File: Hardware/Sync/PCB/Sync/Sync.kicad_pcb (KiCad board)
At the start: 2 copper layers, 50.8 x 35.6 mm, 14 parts, among them J1 Conn_01x04_Male, J2 Conn_01x02_Pin, J3 AudioJack3, J4 AudioJack3, Q1 2N3904, Q2 2N3904

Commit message: Updates
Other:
- board size 50.8 x 35.6 mm -> 48.3 x 27.9 mm
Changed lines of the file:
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@@
 		)
-	)
-	(gr_circle
-		(center 134.62 43.18)
-		(end 136.12 43.18)
-		(stroke
-			(width 0.1)
-			(type solid)
-		)
-		(fill none)
-		(layer "Edge.Cuts")
-	)
-	(gr_circle
-		(center 88.9 73.66)
-		(end 90.4 73.66)
-		(stroke
-			(width 0.1)
-			(type solid)
-		)
-		(fill none)
-		(layer "Edge.Cuts")
-	)
-	(gr_circle
-		(center 88.9 43.18)
-		(end 90.4 43.18)
-		(stroke
-			(width 0.1)
-			(type solid)
-		)
-		(fill none)
-		(layer "Edge.Cuts")
-	)
-	(gr_circle
-		(center 134.62 73.66)
-		(end 136.12 73.66)
-		(stroke
-			(width 0.1)
-			(type solid)
-		)
-		(fill none)
-		(layer "Edge.Cuts")
 	)
 	(gr_rect
-		(start 86.36 40.64)
-		(end 137.16 76.2)
+		(start 88.9 44.45)
+		(end 137.16 72.39)
 		(stroke
 			(width 0.05)
@@
 		)
 	)
-	(gr_text "SYNC"
-		(at 96.52 72.39 0)
-		(layer "F.SilkS")
-		(effects
-			(font
-				(size 1 1)
-				(thickness 0.15)
-			)
-			(justify bottom)
-		)
-	)
 	(gr_text "SYNC_IN"
 		(at 98.425 50.165 0)
@@
 	)
 	(gr_text "SYNC"
-		(at 113.03 73.66 0)
+		(at 102.87 71.12 0)
 		(layer "F.SilkS")
 		(effects
@@
 		(polygon
 			(pts
-				(xy 88.9 43.18) (xy 88.9 73.66) (xy 134.62 73.66) (xy 134.62 43.18)
-			)
-		)
+				(xy 88.9 44.45) (xy 88.9 72.39) (xy 137.16 72.39) (xy 137.16 44.45)
+			)
+		)

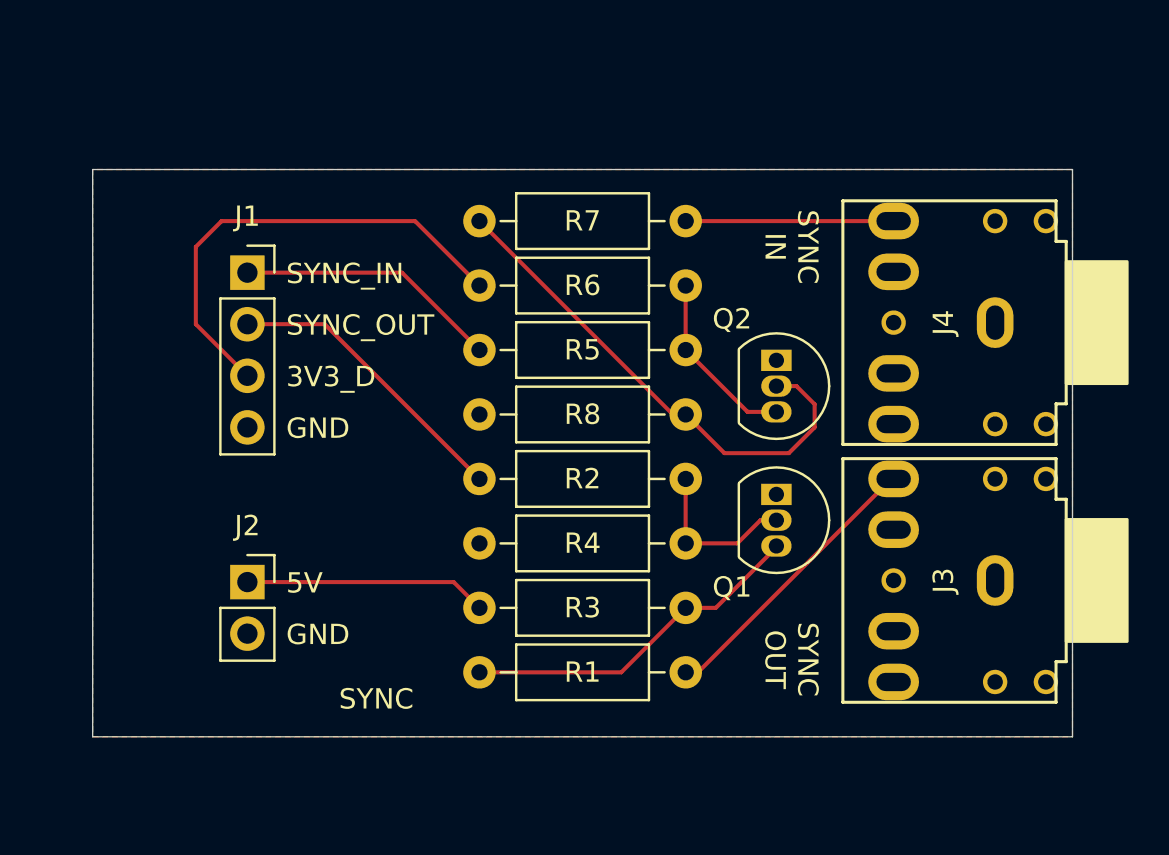
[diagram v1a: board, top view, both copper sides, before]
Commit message: Edges removed
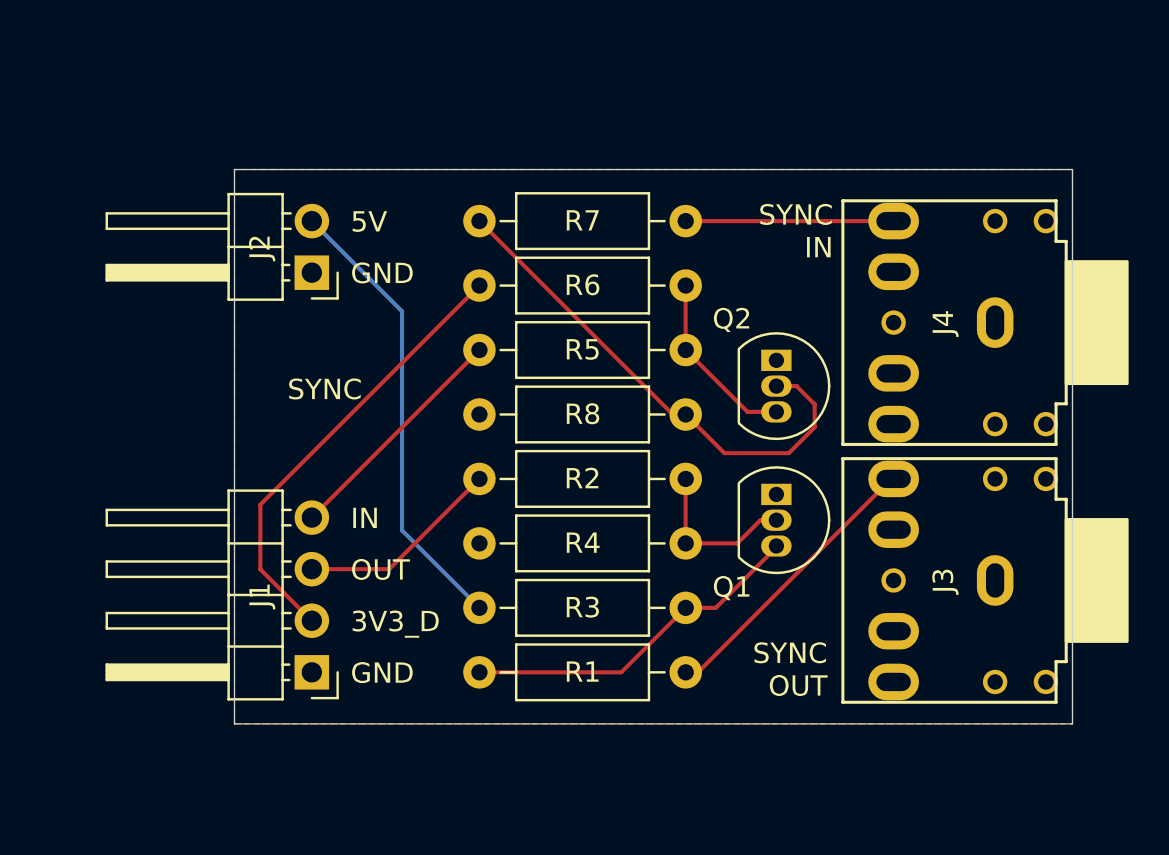
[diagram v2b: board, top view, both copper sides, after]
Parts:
- J1: footprint Connector_PinSocket_2.54mm:PinSocket_1x04_P2.54mm_Vertical -> Connector_PinHeader_2.54mm:PinHeader_1x04_P2.54mm_Horizontal
- J2: footprint Connector_PinSocket_2.54mm:PinSocket_1x02_P2.54mm_Vertical -> Connector_PinHeader_2.54mm:PinHeader_1x02_P2.54mm_Horizontal
- moved J1 19.9 mm to (99.7, 69.2), turned to 180 degrees
- moved J2 15.6 mm to (99.7, 49.5), turned to 180 degrees
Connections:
- J1 pad 1: SYNC_IN -> GND
- J1 pad 2: SYNC_OUT -> 3V3_D
- J1 pad 3: 3V3_D -> SYNC_OUT
- J1 pad 4: GND -> SYNC_IN
- J2 pad 1: 5V -> GND
- J2 pad 2: GND -> 5V
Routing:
- net 5V: track 12.0 -> 22.5 mm
- net SYNC_OUT: track 14.6 -> 10.1 mm
- net SYNC_IN: track 13.0 -> 11.7 mm
- net 3V3_D: track 23.2 -> 22.0 mm
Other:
- board size 48.3 x 27.9 mm -> 41.3 x 27.3 mm
- board text added: "IN"
- board text added: "OUT"
- board text removed: "SYNC_IN"
- board text removed: "SYNC_OUT"

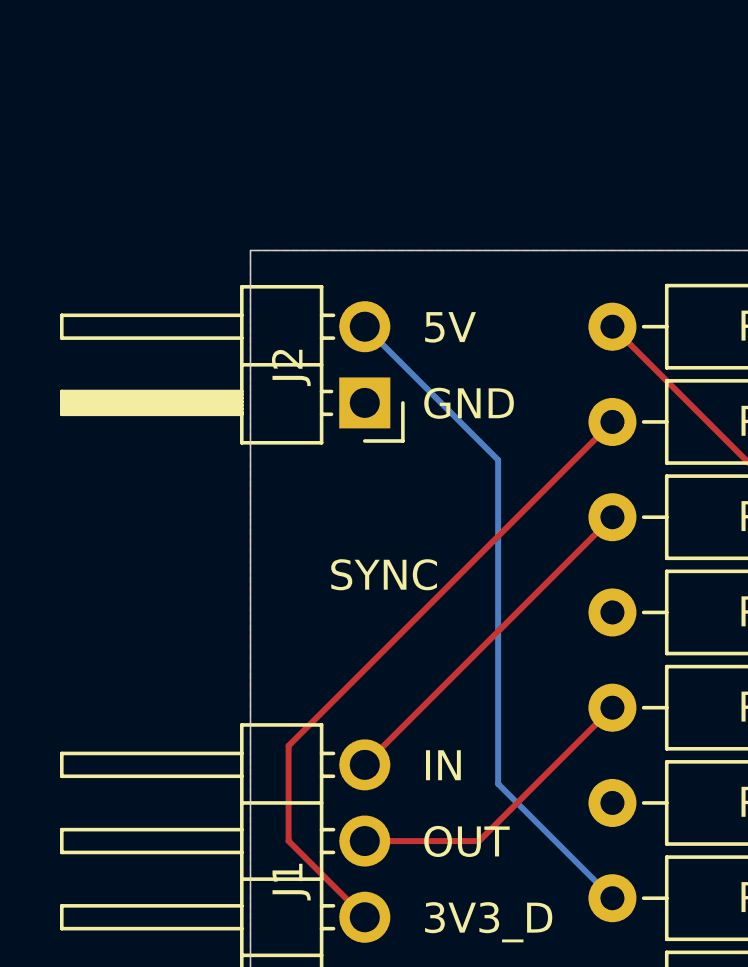
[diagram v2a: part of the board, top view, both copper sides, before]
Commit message: Added PSU
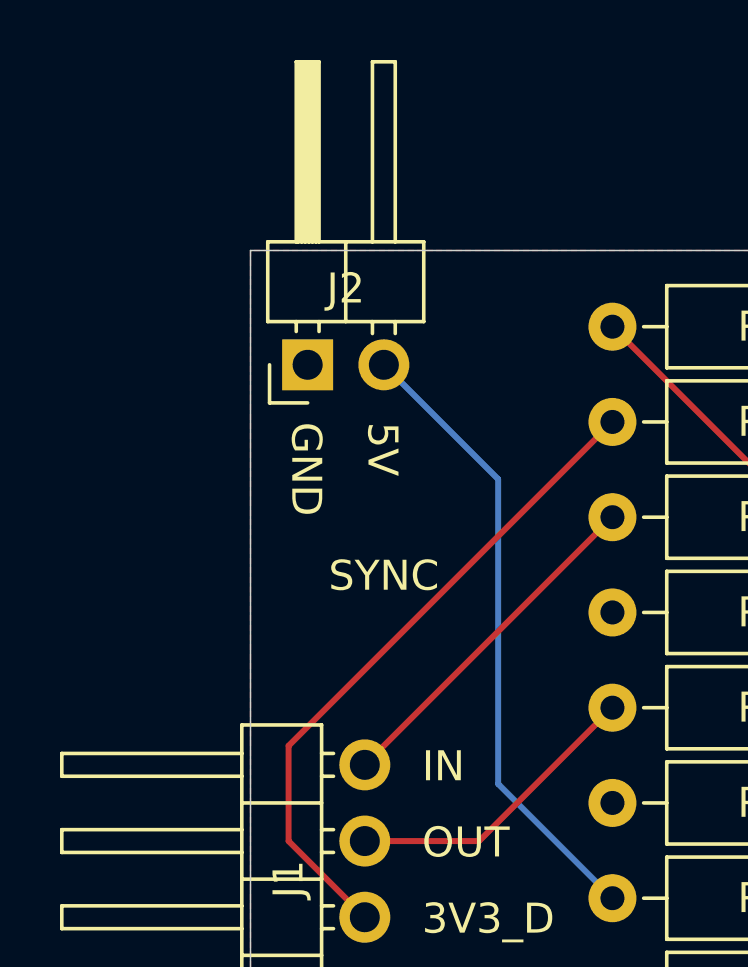
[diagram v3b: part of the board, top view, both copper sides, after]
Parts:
- moved J2 2.29 mm to (97.8, 48.3), turned to 90 degrees
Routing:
- net 5V: track 22.5 -> 20.9 mm
